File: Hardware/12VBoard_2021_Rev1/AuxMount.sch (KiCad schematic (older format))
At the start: 35 parts, among them Q4 2N7000, Q5 2N7000, U10 LM5116, U11 INA198, U17 LM2576S-12/NOPB

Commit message: Missing footprints issue found
Library difference between computer caused footprints not to appear on the layout
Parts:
- R38: footprint Resistor_SMD:R_0603_1608Metric_Pad0.98x0.95mm_HandSolder -> Resistor_SMD:R_0603_1608Metric_Pad1.05x0.95mm_HandSolder
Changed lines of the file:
@@
 F 0 "R38" H 9070 2421 50  0000 L CNN
 F 1 "1.2k" H 9070 2330 50  0000 L CNN
-F 2 "Resistor_SMD:R_0603_1608Metric_Pad0.98x0.95mm_HandSolder" V 8930 2375 50  0001 C CNN
+F 2 "Resistor_SMD:R_0603_1608Metric_Pad1.05x0.95mm_HandSolder" V 8930 2375 50  0001 C CNN
 F 3 "~" H 9000 2375 50  0001 C CNN
 	1    9000 2375

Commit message: Fixed Resistor and Capasitor footprints
found other issues
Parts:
- C23, C24, C25, C26, C28, C29, C31, C32: footprint Capacitor_SMD:C_0603_1608Metric_Pad1.08x0.95mm_HandSolder -> Capacitor_SMD:C_0603_1608Metric_Pad1.05x0.95mm_HandSolder
- R19, R20, R21, R22, R23, R24, R26: footprint Resistor_SMD:R_0603_1608Metric_Pad0.98x0.95mm_HandSolder -> Resistor_SMD:R_0603_1608Metric_Pad1.05x0.95mm_HandSolder
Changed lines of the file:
@@
 F 0 "R26" H 4020 3846 50  0000 L CNN
 F 1 "1.2k" H 4020 3755 50  0000 L CNN
-F 2 "Resistor_SMD:R_0603_1608Metric_Pad0.98x0.95mm_HandSolder" V 3880 3800 50  0001 C CNN
+F 2 "Resistor_SMD:R_0603_1608Metric_Pad1.05x0.95mm_HandSolder" V 3880 3800 50  0001 C CNN
 F 3 "~" H 3950 3800 50  0001 C CNN
 	1    3950 3800
@@
 F 0 "R24" H 2259 2196 50  0000 L CNN
 F 1 "261K" H 2259 2105 50  0000 L CNN
-F 2 "Resistor_SMD:R_0603_1608Metric_Pad0.98x0.95mm_HandSolder" H 2200 2150 50  0001 C CNN
+F 2 "Resistor_SMD:R_0603_1608Metric_Pad1.05x0.95mm_HandSolder" H 2200 2150 50  0001 C CNN
 F 3 "~" H 2200 2150 50  0001 C CNN
 	1    2200 2150
@@
 F 0 "R20" H 1459 996 50  0000 L CNN
 F 1 "36.5K" H 1459 905 50  0000 L CNN
-F 2 "Resistor_SMD:R_0603_1608Metric_Pad0.98x0.95mm_HandSolder" H 1400 950 50  0001 C CNN
+F 2 "Resistor_SMD:R_0603_1608Metric_Pad1.05x0.95mm_HandSolder" H 1400 950 50  0001 C CNN
 F 3 "~" H 1400 950 50  0001 C CNN
 	1    1400 950
@@
 F 0 "R21" H 1459 1296 50  0000 L CNN
 F 1 "2.26K" H 1459 1205 50  0000 L CNN
-F 2 "Resistor_SMD:R_0603_1608Metric_Pad0.98x0.95mm_HandSolder" H 1400 1250 50  0001 C CNN
+F 2 "Resistor_SMD:R_0603_1608Metric_Pad1.05x0.95mm_HandSolder" H 1400 1250 50  0001 C CNN
 F 3 "~" H 1400 1250 50  0001 C CNN
 	1    1400 1250
@@
 F 0 "R23" H 1759 4696 50  0000 L CNN
 F 1 "9.76K" H 1759 4605 50  0000 L CNN
-F 2 "Resistor_SMD:R_0603_1608Metric_Pad0.98x0.95mm_HandSolder" H 1700 4650 50  0001 C CNN
+F 2 "Resistor_SMD:R_0603_1608Metric_Pad1.05x0.95mm_HandSolder" H 1700 4650 50  0001 C CNN
 F 3 "~" H 1700 4650 50  0001 C CNN
 	1    1700 4650
@@
 F 0 "R22" H 1759 4396 50  0000 L CNN
 F 1 "86.6K" H 1759 4305 50  0000 L CNN
-F 2 "Resistor_SMD:R_0603_1608Metric_Pad0.98x0.95mm_HandSolder" H 1700 4350 50  0001 C CNN
+F 2 "Resistor_SMD:R_0603_1608Metric_Pad1.05x0.95mm_HandSolder" H 1700 4350 50  0001 C CNN
 F 3 "~" H 1700 4350 50  0001 C CNN
 	1    1700 4350
@@
 F 0 "R19" H 1259 4296 50  0000 L CNN
 F 1 "5m" H 1259 4205 50  0000 L CNN
-F 2 "Resistor_SMD:R_0603_1608Metric_Pad0.98x0.95mm_HandSolder" H 1200 4250 50  0001 C CNN
+F 2 "Resistor_SMD:R_0603_1608Metric_Pad1.05x0.95mm_HandSolder" H 1200 4250 50  0001 C CNN
 F 3 "~" H 1200 4250 50  0001 C CNN
 	1    1200 4250
@@
 F 0 "C24" H 1092 1046 50  0000 L CNN
 F 1 "2.2uF" H 1092 955 50  0000 L CNN
-F 2 "Capacitor_SMD:C_0603_1608Metric_Pad1.08x0.95mm_HandSolder" H 1000 1000 50  0001 C CNN
+F 2 "Capacitor_SMD:C_0603_1608Metric_Pad1.05x0.95mm_HandSolder" H 1000 1000 50  0001 C CNN
 F 3 "~" H 1000 1000 50  0001 C CNN
 	1    1000 1000
@@
 F 0 "C26" H 1292 1046 50  0000 L CNN
 F 1 "100nF" H 1292 955 50  0000 L CNN
-F 2 "Capacitor_SMD:C_0603_1608Metric_Pad1.08x0.95mm_HandSolder" H 1200 1000 50  0001 C CNN
+F 2 "Capacitor_SMD:C_0603_1608Metric_Pad1.05x0.95mm_HandSolder" H 1200 1000 50  0001 C CNN
 F 3 "~" H 1200 1000 50  0001 C CNN
 	1    1200 1000
@@
 F 0 "C31" V 2121 1200 50  0000 C CNN
 F 1 "470pF" V 2212 1200 50  0000 C CNN
-F 2 "Capacitor_SMD:C_0603_1608Metric_Pad1.08x0.95mm_HandSolder" H 2350 1200 50  0001 C CNN
+F 2 "Capacitor_SMD:C_0603_1608Metric_Pad1.05x0.95mm_HandSolder" H 2350 1200 50  0001 C CNN
 F 3 "~" H 2350 1200 50  0001 C CNN
 	1    2350 1200
@@
 F 0 "C32" V 2121 1400 50  0000 C CNN
 F 1 "33nF" V 2212 1400 50  0000 C CNN
-F 2 "Capacitor_SMD:C_0603_1608Metric_Pad1.08x0.95mm_HandSolder" H 2350 1400 50  0001 C CNN
+F 2 "Capacitor_SMD:C_0603_1608Metric_Pad1.05x0.95mm_HandSolder" H 2350 1400 50  0001 C CNN
 F 3 "~" H 2350 1400 50  0001 C CNN
 	1    2350 1400
@@
 F 0 "C28" H 2142 1946 50  0000 L CNN
 F 1 "10pF" H 2142 1855 50  0000 L CNN
-F 2 "Capacitor_SMD:C_0603_1608Metric_Pad1.08x0.95mm_HandSolder" H 2050 1900 50  0001 C CNN
+F 2 "Capacitor_SMD:C_0603_1608Metric_Pad1.05x0.95mm_HandSolder" H 2050 1900 50  0001 C CNN
 F 3 "~" H 2050 1900 50  0001 C CNN
 	1    2050 1900
@@
 F 0 "C29" H 2292 1946 50  0000 L CNN
 F 1 "120pF" H 2292 1855 50  0000 L CNN
-F 2 "Capacitor_SMD:C_0603_1608Metric_Pad1.08x0.95mm_HandSolder" H 2200 1900 50  0001 C CNN
+F 2 "Capacitor_SMD:C_0603_1608Metric_Pad1.05x0.95mm_HandSolder" H 2200 1900 50  0001 C CNN
 F 3 "~" H 2200 1900 50  0001 C CNN
 	1    2200 1900
@@
 F 0 "C25" H 1192 2746 50  0000 L CNN
 F 1 "1uF" H 1192 2655 50  0000 L CNN
-F 2 "Capacitor_SMD:C_0603_1608Metric_Pad1.08x0.95mm_HandSolder" H 1100 2700 50  0001 C CNN
+F 2 "Capacitor_SMD:C_0603_1608Metric_Pad1.05x0.95mm_HandSolder" H 1100 2700 50  0001 C CNN
 F 3 "~" H 1100 2700 50  0001 C CNN
 	1    1100 2700
@@
 F 0 "C23" H 1042 3046 50  0000 L CNN
 F 1 "100nF" H 1042 2955 50  0000 L CNN
-F 2 "Capacitor_SMD:C_0603_1608Metric_Pad1.08x0.95mm_HandSolder" H 950 3000 50  0001 C CNN
+F 2 "Capacitor_SMD:C_0603_1608Metric_Pad1.05x0.95mm_HandSolder" H 950 3000 50  0001 C CNN
 F 3 "~" H 950 3000 50  0001 C CNN
 	1    950  3000

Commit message: Components
Added the correct mosfets for the extra and the high current bucks
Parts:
- removed Q4, Q5: 2N7000, Package_TO_SOT_THT:TO-92_Inline, symbol Transistor_FET:2N7000
- added Q4: CSD18537NQ5A, symbol 12VBoard_2021_Rev1-rescue:CSD18537NQ5A
- added Q5: CSD18531Q5A, symbol 12VBoard_2021_Rev1-rescue:CSD18531Q5A
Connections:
- wire segments 150 -> 172
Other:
- moved on the sheet: R19
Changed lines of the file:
@@
 L power:GND #PWR?
 U 1 1 5FE32FF4
-P 1200 4450
+P 1225 4850
 AR Path="/5F74F36B/5F971CD6/5FE32FF4" Ref="#PWR?"  Part="1"
 AR Path="/5F74F36B/5F8222BE/5FE32FF4" Ref="#PWR057"  Part="1"
-F 0 "#PWR057" H 1200 4200 50  0001 C CNN
-F 1 "GND" H 1205 4277 50  0000 C CNN
-F 2 "" H 1200 4450 50  0001 C CNN
-F 3 "" H 1200 4450 50  0001 C CNN
-	1    1200 4450
+F 0 "#PWR057" H 1225 4600 50  0001 C CNN
+F 1 "GND" H 1230 4677 50  0000 C CNN
+F 2 "" H 1225 4850 50  0001 C CNN
+F 3 "" H 1225 4850 50  0001 C CNN
+	1    1225 4850
 	1    0    0    -1
 $EndComp
@@
 Wire Wire Line
 	1100 2800 1100 2850
-Text HLabel 1250 3100 2    50   Input ~ 0
+Text HLabel 1750 2900 2    50   Input ~ 0
 PackVoltage
-$Comp
-L Transistor_FET:2N7000 Q?
-U 1 1 5FE33020
-P 1050 3350
-AR Path="/5F74F36B/5F971CD6/5FE33020" Ref="Q?"  Part="1"
-AR Path="/5F74F36B/5F8222BE/5FE33020" Ref="Q4"  Part="1"
-F 0 "Q4" H 1254 3396 50  0000 L CNN
-F 1 "2N7000" H 1254 3305 50  0000 L CNN
-F 2 "Package_TO_SOT_THT:TO-92_Inline" H 1250 3275 50  0001 L CIN
-F 3 "https://www.fairchildsemi.com/datasheets/2N/2N7000.pdf" H 1050 3350 50  0001 L CNN
-	1    1050 3350
-	1    0    0    -1
-$EndComp
-Wire Wire Line
-	1250 3100 1150 3100
-Wire Wire Line
-	1150 3100 1150 3150
-$Comp
-L Transistor_FET:2N7000 Q?
-U 1 1 5FE33028
-P 1100 3850
-AR Path="/5F74F36B/5F971CD6/5FE33028" Ref="Q?"  Part="1"
-AR Path="/5F74F36B/5F8222BE/5FE33028" Ref="Q5"  Part="1"
-F 0 "Q5" H 1304 3896 50  0000 L CNN
-F 1 "2N7000" H 1304 3805 50  0000 L CNN
-F 2 "Package_TO_SOT_THT:TO-92_Inline" H 1300 3775 50  0001 L CIN
-F 3 "https://www.fairchildsemi.com/datasheets/2N/2N7000.pdf" H 1100 3850 50  0001 L CNN
-	1    1100 3850
-	1    0    0    -1
-$EndComp
-Wire Wire Line
-	1150 3550 1150 3600
 Wire Wire Line
 	1150 3600 1200 3600
-Wire Wire Line
-	1200 3600 1200 3650
 Wire Wire Line
 	950  3100 950  3600
@@
 L Device:R_Small R?
 U 1 1 5FE3303C
-P 1200 4250
+P 1225 4650
 AR Path="/5F74F36B/5F971CD6/5FE3303C" Ref="R?"  Part="1"
 AR Path="/5F74F36B/5F8222BE/5FE3303C" Ref="R19"  Part="1"
-F 0 "R19" H 1259 4296 50  0000 L CNN
-F 1 "5m" H 1259 4205 50  0000 L CNN
-F 2 "Resistor_SMD:R_0603_1608Metric_Pad1.05x0.95mm_HandSolder" H 1200 4250 50  0001 C CNN
-F 3 "~" H 1200 4250 50  0001 C CNN
-	1    1200 4250
-	1    0    0    -1
-$EndComp
-Wire Wire Line
-	1200 4050 1200 4100
-Wire Wire Line
-	1200 4350 1200 4400
-Text GLabel 800  3350 0    50   Input ~ 0
+F 0 "R19" H 1284 4696 50  0000 L CNN
+F 1 "5m" H 1284 4605 50  0000 L CNN
+F 2 "Resistor_SMD:R_0603_1608Metric_Pad1.05x0.95mm_HandSolder" H 1225 4650 50  0001 C CNN
+F 3 "~" H 1225 4650 50  0001 C CNN
+	1    1225 4650
+	1    0    0    -1
+$EndComp
+Wire Wire Line
+	1225 4750 1225 4800
+Text GLabel 1700 3400 3    50   Input ~ 0
 HO
-Text GLabel 850  3850 0    50   Input ~ 0
+Text GLabel 1525 4250 3    50   Input ~ 0
 LO
-Wire Wire Line
-	850  3350 800  3350
-Wire Wire Line
-	900  3850 850  3850
 Wire Wire Line
 	950  2800 950  2850
@@
 Wire Wire Line
 	950  2600 950  2550
-Text GLabel 1150 4100 0    50   Input ~ 0
+Text GLabel 1175 4500 0    50   Input ~ 0
 CS
-Text GLabel 1150 4400 0    50   Input ~ 0
+Text GLabel 1175 4800 0    50   Input ~ 0
 CSGDEMB
 Wire Wire Line
-	1200 4100 1150 4100
-Connection ~ 1200 4100
-Wire Wire Line
-	1200 4100 1200 4150
-Wire Wire Line
-	1200 4400 1150 4400
-Connection ~ 1200 4400
-Wire Wire Line
-	1200 4400 1200 4450
+	1225 4500 1175 4500
+Connection ~ 1225 4500
+Wire Wire Line
+	1225 4500 1225 4550
+Wire Wire Line
+	1225 4800 1175 4800
+Connection ~ 1225 4800
+Wire Wire Line
+	1225 4800 1225 4850
 $Comp
 L Device:CP1_Small C?
@@
 Text HLabel 5750 1450 0    49   Input ~ 0
 CTL_AuxMount
+$Comp
+L 12VBoard_2021_Rev1-rescue:CSD18537NQ5A Q?
+U 1 1 5FC66883
+P 1550 3150
+AR Path="/5F74F36B/5F8236F9/5FC66883" Ref="Q?"  Part="1"
+AR Path="/5F74F36B/5F8222BE/5FC66883" Ref="Q4"  Part="1"
+F 0 "Q4" V 1475 2925 50  0000 R CNN
+F 1 "CSD18537NQ5A" V 1600 2950 50  0000 R CNN
+F 2 "" H 1550 3150 50  0001 C CNN
+F 3 "" H 1550 3150 50  0001 C CNN
+	1    1550 3150
+	0    -1   -1   0
+$EndComp
+$Comp
+L 12VBoard_2021_Rev1-rescue:CSD18531Q5A Q?
+U 1 1 5FC66889
+P 1375 4000
+AR Path="/5F74F36B/5F8236F9/5FC66889" Ref="Q?"  Part="1"
+AR Path="/5F74F36B/5F8222BE/5FC66889" Ref="Q5"  Part="1"
+F 0 "Q5" V 1325 4325 50  0000 R CNN
+F 1 "CSD18531Q5A" V 1400 4750 50  0000 R CNN
+F 2 "" H 1375 4050 50  0001 C CNN
+F 3 "" H 1375 4050 50  0001 C CNN
+	1    1375 4000
+	0    -1   -1   0
+$EndComp
+Wire Wire Line
+	1600 3350 1500 3350
+Wire Wire Line
+	1400 3350 1500 3350
+Connection ~ 1500 3350
+Wire Wire Line
+	1700 2900 1600 2900
+Wire Wire Line
+	1400 2900 1400 2950
+Wire Wire Line
+	1500 2950 1500 2900
+Connection ~ 1500 2900
+Wire Wire Line
+	1500 2900 1400 2900
+Wire Wire Line
+	1600 2950 1600 2900
+Connection ~ 1600 2900
+Wire Wire Line
+	1600 2900 1500 2900
+Wire Wire Line
+	1700 2950 1700 2900
+Wire Wire Line
+	1700 2900 1750 2900
+Connection ~ 1700 2900
+Wire Wire Line
+	1400 3350 1150 3350
+Wire Wire Line
+	1150 3350 1150 3600
+Connection ~ 1400 3350
+Wire Wire Line
+	1225 4250 1225 4500
+Connection ~ 1225 4250
+Wire Wire Line
+	1225 4200 1225 4250
+Wire Wire Line
+	1325 4200 1325 4250
+Connection ~ 1325 4250
+Wire Wire Line
+	1325 4250 1225 4250
+Wire Wire Line
+	1425 4200 1425 4250
+Wire Wire Line
+	1425 4250 1325 4250
+Wire Wire Line
+	1525 4250 1525 4200
+Wire Wire Line
+	1200 3750 1225 3750
+Wire Wire Line
+	1525 3750 1525 3800
+Wire Wire Line
+	1200 3600 1200 3750
+Wire Wire Line
+	1425 3800 1425 3750
+Connection ~ 1425 3750
+Wire Wire Line
+	1425 3750 1525 3750
+Wire Wire Line
+	1325 3800 1325 3750
+Connection ~ 1325 3750
+Wire Wire Line
+	1325 3750 1425 3750
+Wire Wire Line
+	1225 3800 1225 3750
+Connection ~ 1225 3750
+Wire Wire Line
+	1225 3750 1325 3750
+Wire Wire Line
+	1700 3400 1700 3350
 $EndSCHEMATC

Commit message: updated footprints
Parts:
- D25: footprint Diode_SMD:D_0603_1608Metric_Pad1.05x0.95mm_HandSolder -> Diode_THT:D_DO-201AD_P15.24mm_Horizontal
- Q4, Q5: footprint (none) -> Package_SON:VSONP-8-1EP_5x6_P1.27mm
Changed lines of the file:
@@
 F 0 "D25" V 7554 1755 50  0000 L CNN
 F 1 "D_Schottky" V 7645 1755 50  0000 L CNN
-F 2 "Diode_SMD:D_0603_1608Metric_Pad1.05x0.95mm_HandSolder" H 7600 1675 50  0001 C CNN
+F 2 "Diode_THT:D_DO-201AD_P15.24mm_Horizontal" H 7600 1675 50  0001 C CNN
 F 3 "~" H 7600 1675 50  0001 C CNN
 	1    7600 1675
@@
 F 0 "Q4" V 1475 2925 50  0000 R CNN
 F 1 "CSD18537NQ5A" V 1600 2950 50  0000 R CNN
-F 2 "" H 1550 3150 50  0001 C CNN
+F 2 "Package_SON:VSONP-8-1EP_5x6_P1.27mm" H 1550 3150 50  0001 C CNN
 F 3 "" H 1550 3150 50  0001 C CNN
 	1    1550 3150
@@
 F 0 "Q5" V 1325 4325 50  0000 R CNN
 F 1 "CSD18531Q5A" V 1400 4750 50  0000 R CNN
-F 2 "" H 1375 4050 50  0001 C CNN
+F 2 "Package_SON:VSONP-8-1EP_5x6_P1.27mm" H 1375 4050 50  0001 C CNN
 F 3 "" H 1375 4050 50  0001 C CNN
 	1    1375 4000

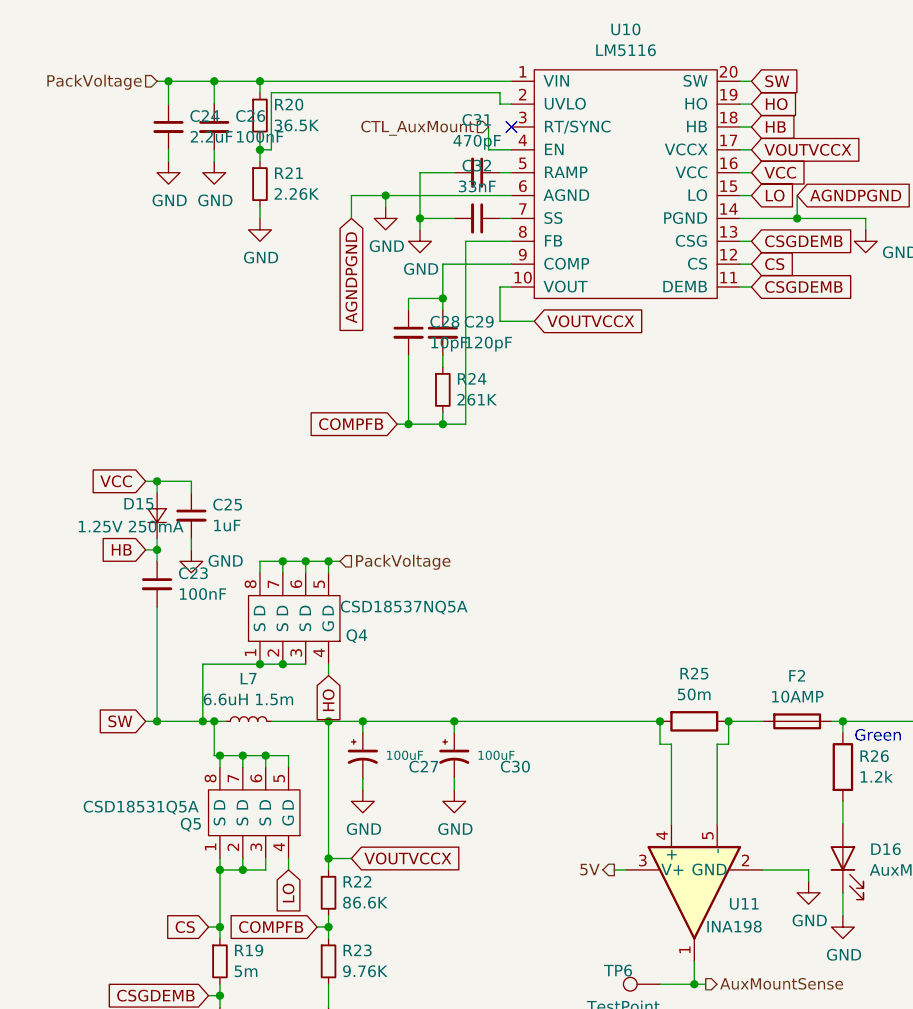
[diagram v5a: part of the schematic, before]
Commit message: Checked H pins
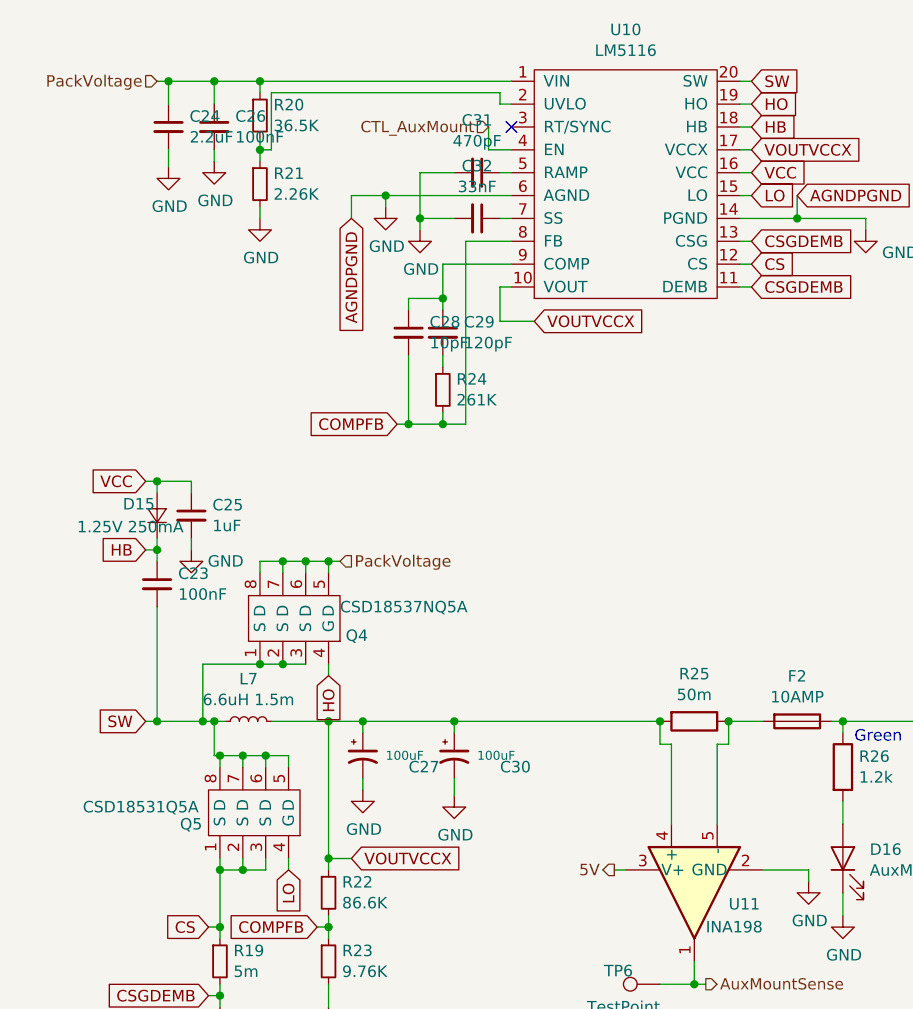
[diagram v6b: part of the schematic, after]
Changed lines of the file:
@@
 EESchema Schematic File Version 4
-LIBS:12VBoard_2021_Rev1-cache
 EELAYER 30 0
 EELAYER END
 $Descr A4 11693 8268
 encoding utf-8
-Sheet 6 8
+Sheet 4 8
 Title ""
 Date ""
@@
 HB
 Wire Wire Line
-	3550 1300 3500 1300
-Wire Wire Line
 	3550 900  3500 900
 Text GLabel 3550 900  2    50   Input ~ 0
@@
 	1000 800  1200 800
 $Comp
-L power:GND #PWR?
-U 1 1 5FA7E754
-P 1000 1150
-AR Path="/5F74F36B/5F971CD6/5FA7E754" Ref="#PWR?"  Part="1"
-AR Path="/5F74F36B/5F8222BE/5FA7E754" Ref="#PWR054"  Part="1"
-F 0 "#PWR054" H 1000 900 50  0001 C CNN
-F 1 "GND" H 1005 977 50  0000 C CNN
-F 2 "" H 1000 1150 50  0001 C CNN
-F 3 "" H 1000 1150 50  0001 C CNN
-	1    1000 1150
-	1    0    0    -1
-$EndComp
-Wire Wire Line
-	1000 1100 1000 1150
-$Comp
 L Device:CP1_Small C?
 U 1 1 5FA837BD
@@
 	1    0    0    -1
 $EndComp
-$Comp
-L power:GND #PWR?
-U 1 1 5FA83CBC
-P 2250 3900
-AR Path="/5F74F36B/5F971CD6/5FA83CBC" Ref="#PWR?"  Part="1"
-AR Path="/5F74F36B/5F8222BE/5FA83CBC" Ref="#PWR063"  Part="1"
-F 0 "#PWR063" H 2250 3650 50  0001 C CNN
-F 1 "GND" H 2255 3727 50  0000 C CNN
-F 2 "" H 2250 3900 50  0001 C CNN
-F 3 "" H 2250 3900 50  0001 C CNN
-	1    2250 3900
-	1    0    0    -1
-$EndComp
-Wire Wire Line
-	2250 3900 2250 3850
 Wire Wire Line
 	2250 3650 2250 3600
@@
 Wire Wire Line
 	1700 3400 1700 3350
+Wire Wire Line
+	3500 1300 3550 1300
+$Comp
+L power:GND #PWR?
+U 1 1 5FA83CBC
+P 2250 3925
+AR Path="/5F74F36B/5F971CD6/5FA83CBC" Ref="#PWR?"  Part="1"
+AR Path="/5F74F36B/5F8222BE/5FA83CBC" Ref="#PWR063"  Part="1"
+F 0 "#PWR063" H 2250 3675 50  0001 C CNN
+F 1 "GND" H 2255 3752 50  0000 C CNN
+F 2 "" H 2250 3925 50  0001 C CNN
+F 3 "" H 2250 3925 50  0001 C CNN
+	1    2250 3925
+	1    0    0    -1
+$EndComp
+Wire Wire Line
+	2250 3850 2250 3925
+$Comp
+L power:GND #PWR0101
+U 1 1 5FC092BD
+P 1000 1175
+F 0 "#PWR0101" H 1000 925 50  0001 C CNN
+F 1 "GND" H 1005 1002 50  0000 C CNN
+F 2 "" H 1000 1175 50  0001 C CNN
+F 3 "" H 1000 1175 50  0001 C CNN
+	1    1000 1175
+	1    0    0    -1
+$EndComp
+Wire Wire Line
+	1000 1100 1000 1175
 $EndSCHEMATC

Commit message: Lunch Break
Routing thinzs
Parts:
- D25: footprint Diode_THT:D_DO-201AD_P15.24mm_Horizontal -> Diode_THT:D_DO-201AD_P5.08mm_Vertical_KathodeUp
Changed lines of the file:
@@
 F 0 "D25" V 7554 1755 50  0000 L CNN
 F 1 "D_Schottky" V 7645 1755 50  0000 L CNN
-F 2 "Diode_THT:D_DO-201AD_P15.24mm_Horizontal" H 7600 1675 50  0001 C CNN
+F 2 "Diode_THT:D_DO-201AD_P5.08mm_Vertical_KathodeUp" H 7600 1675 50  0001 C CNN
 F 3 "~" H 7600 1675 50  0001 C CNN
 	1    7600 1675
@@
 AR Path="/5F74F36B/5F8236F9/5FC66889" Ref="Q?"  Part="1"
 AR Path="/5F74F36B/5F8222BE/5FC66889" Ref="Q5"  Part="1"
+AR Path="/5FC66889" Ref="Q5"  Part="1"
 F 0 "Q5" V 1325 4325 50  0000 R CNN
 F 1 "CSD18531Q5A" V 1400 4750 50  0000 R CNN
